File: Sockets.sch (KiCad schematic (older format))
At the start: 1 part

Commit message: Added Input Limit Switch
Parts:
- added C? (x4): C, symbol Device:C
- added D? (x2): SK35SMA, Diode_SMD:D_SMA, symbol Device:D_ALT
- added J?: LIMIT Y FRONT, Connector_JST:JST_PH_B2B-PH-K_1x02_P2.00mm_Vertical, symbol Connector:Conn_01x02_Male
- added J?: LIMIT Z UP, Connector_JST:JST_PH_B2B-PH-K_1x02_P2.00mm_Vertical, symbol Connector:Conn_01x02_Male
- added J?: LIMIT Z DOWN, Connector_JST:JST_PH_B2B-PH-K_1x02_P2.00mm_Vertical, symbol Connector:Conn_01x02_Male
- added J?: WASTE INK, Connector_JST:JST_PH_B2B-PH-K_1x02_P2.00mm_Vertical, symbol Connector:Conn_01x02_Male
- added J?: PRINTER POWER, Connector_JST:JST_PH_B2B-PH-K_1x02_P2.00mm_Vertical, symbol Connector:Conn_01x02_Male
- added J?: PE SENSOR, Connector_JST:JST_PH_B2B-PH-K_1x02_P2.00mm_Vertical, symbol Connector:Conn_01x02_Male
- added J?: LED 1, Connector_JST:JST_PH_B2B-PH-K_1x03_P2.00mm_Vertical, symbol Connector:Conn_01x03_Male
- added J?: LED 2, Connector_JST:JST_PH_B2B-PH-K_1x03_P2.00mm_Vertical, symbol Connector:Conn_01x03_Male
- added R? (x4): 1kΩ, Resistor_SMD:R_0603_1608Metric, symbol Device:R
- added R? (x4): 100kΩ, Resistor_SMD:R_0603_1608Metric, symbol Device:R
- added R? (x2): 330Ω, symbol Device:R
- added U?: 74HC245, symbol 74xx:74HC245
- J?: value Conn_01x03_Male -> LIMIT Y BACK; footprint (none) -> Connector_JST:JST_PH_B2B-PH-K_1x02_P2.00mm_Vertical; symbol Connector:Conn_01x03_Male -> Connector:Conn_01x02_Male
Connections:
- net at J?.1 (Pin_1): now also R?.1
- net GND: now reaches J?.2 (Pin_2)
- net GND: now also C?.2, C?.2, C?.2, C?.2, J?.2 (Pin_2), J?.2 (Pin_2), J?.2 (Pin_2), J?.3 (Pin_3), J?.3 (Pin_3)
- new net: J?.1 (Pin_1), R?.1 (x3)
- new net: D?.1 (K), J?.1 (Pin_1) (x2)
- new net: J?.2 (Pin_2), R?.2 (x2)
- new net +3V3: R?.2, R?.2, R?.2, R?.2
- new net +5V: D?.2 (A), D?.2 (A)
- new net LED1_CONTROL: R?.1
- new net LED2_CONTROL: R?.1
- new net LIMIT_Y_BACK: C?.1, R?.1, R?.2
- new net LIMIT_Y_FRONT: C?.1, R?.1, R?.2
- new net LIMIT_Z_DOWN: C?.1, R?.1, R?.2
- new net LIMIT_Z_UP: C?.1, R?.1, R?.2
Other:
- note added: "Złącza JST PH"
- note added: "pomyśleć nad buffoerm 74HC245 albo wersja LVC zależy od napięć"
- note added: "sprawdzić jak to podłączyć, jakie napięcia"
- note added: "wykrycie czy drukarka włączaona"
- note removed: "Złącza JST KR"

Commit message: Finished Emergency Circuit
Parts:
- removed C? (x4): C, symbol Device:C
- removed D? (x2): SK35SMA, Diode_SMD:D_SMA, symbol Device:D_ALT
- removed J?: PE SENSOR, Connector_JST:JST_PH_B2B-PH-K_1x02_P2.00mm_Vertical, symbol Connector:Conn_01x02_Male
- removed R? (x4): 1kΩ, Resistor_SMD:R_0603_1608Metric, symbol Device:R
- removed R? (x4): 100kΩ, Resistor_SMD:R_0603_1608Metric, symbol Device:R
- removed R? (x2): 330Ω, symbol Device:R
- added C? (x5): 1nF, Capacitor_SMD:C_0603_1608Metric, symbol Device:C
- added D?: 1N4448WS-7-F, symbol Device:D_ALT
- added D?: BZT52C3V3-7-F, Diode_SMD:D_SOD-123, symbol Device:D_Zener_ALT
- added D? (x2): B140-13-F, symbol Device:D_ALT
- added J?: CA58SUB-B, footprints:THT_FPC_r1.0mm_11pin_vertical, symbol Connector_Generic:Conn_01x11
- added J?: PC6 EPSON MAINBOARD, footprints:THT_FPC_r1.0mm_11pin_vertical, symbol Connector_Generic:Conn_01x11
- added J?: Y AXIS, Connector_JST:JST_PH_B2B-PH-K_1x03_P2.00mm_Vertical, symbol Connector:Conn_01x03_Male
- added J?: Z AXIS, Connector_JST:JST_PH_B2B-PH-K_1x03_P2.00mm_Vertical, symbol Connector:Conn_01x03_Male
- added J?: PHOTO SENSOR EMITER, Connector_JST:JST_PH_B2B-PH-K_1x02_P2.00mm_Vertical, symbol Connector:Conn_01x02_Male
- added J?: PHOTO SENSOR RECEIVER, Connector_JST:JST_PH_B2B-PH-K_1x03_P2.00mm_Vertical, symbol Connector:Conn_01x03_Male
- added Q? (x3): BC817, Package_TO_SOT_SMD:SOT-23, symbol Transistor_BJT:BC817
- added R?: NI, symbol Device:R
- added R? (x2): 0Ω, symbol Device:R
- added R? (x2): 10kΩ, symbol Device:R
- added R? (x3): 4.7kΩ, symbol Device:R
- added R? (x7): 1kΩ, Resistor_SMD:R_0603_1608Metric, symbol Device:R
- added R? (x5): 4.7kΩ, Resistor_SMD:R_0603_1608Metric, symbol Device:R
- added R?: 1kΩ, symbol Device:R
- added R?: NI, Resistor_SMD:R_0603_1608Metric, symbol Device:R
- added R? (x2): 10kΩ, Resistor_SMD:R_0603_1608Metric, symbol Device:R
- added RN? (x2): 330Ω, symbol Device:R_Pack04
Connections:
- net +3V3: now also R?.2, R?.2, R?.2, R?.2, R?.2, R?.2, R?.2
- net +5V: now also U?.1 (A->B), U?.20 (VCC), D?.2 (A), D?.2 (A)
- net GND: now also J?.2 (Pin_2), J?.2 (Pin_2), U?.10 (GND), U?.19 (CE), C?.2, C?.2, C?.2, C?.2, C?.2, D?.2 (A), J?.2 (Pin_2), J?.2 (Pin_2), J?.2 (Pin_2), J?.2 (Pin_2), J?.4 (Pin_4), J?.4 (Pin_4), J?.6 (Pin_6), J?.6 (Pin_6), J?.8 (Pin_8), J?.8 (Pin_8), Q?.2 (E), Q?.2 (E), Q?.2 (E), R?.1
- net LED1_CONTROL: now also U?.6 (A4)
- net LED2_CONTROL: now also U?.7 (A5)
- net LIMIT_Y_BACK: now also C?.1, R?.1
- net LIMIT_Y_FRONT: now also C?.1, R?.1
- net LIMIT_Z_DOWN: now also C?.1, R?.1
- net LIMIT_Z_UP: now also C?.1, R?.1
- net at J?.1 (Pin_1): now also R?.1, R?.2 (x5)
- net at J?.1 (Pin_1): now also R?.2
- net at J?.1 (Pin_1): now also D?.1 (K) (x2)
- net LED1_CNT: now reaches J?.2 (Pin_2)
- net LED1_CNT: now also RN?.4 (R4.1)
- net LED2_CNT: now reaches J?.2 (Pin_2)
- net LED2_CNT: now also RN?.3 (R3.1)
- net at U?.11 (B7): now also RN?.8 (R1.2)
- net at U?.12 (B6): now also RN?.7 (R2.2)
- net at U?.13 (B5): now also RN?.6 (R3.2)
- net at U?.14 (B4): now also RN?.5 (R4.2)
- net at U?.15 (B3): now also RN?.8 (R1.2)
- net at U?.16 (B2): now also RN?.7 (R2.2)
- net at U?.17 (B1): now also RN?.6 (R3.2)
- net at U?.18 (B0): now also RN?.5 (R4.2)
- net Y_STEP: now reaches U?.2 (A0)
- net Y_DIR: now reaches U?.3 (A1)
- net Z_STEP: now reaches U?.4 (A2)
- net Z_DIR: now reaches U?.5 (A3)
- new net: Q?.1 (B), R?.1 (x3)
- new net: D?.1 (K), J?.1 (Pin_1), J?.1 (Pin_1), R?.1
- new net: J?.3 (Pin_3), R?.2, R?.2, R?.2
- new net 3.3V: J?.1 (Pin_1), J?.11 (Pin_11), R?.2
- new net APG: J?.10 (Pin_10), J?.2 (Pin_2)
- new net APGHP: J?.1 (Pin_1), J?.11 (Pin_11)
- new net ENC1_A: R?.1
- new net ENC1_B: R?.1
- new net OPE: J?.3 (Pin_3), Q?.3 (C), R?.1, R?.2
- new net OPF_A: J?.5 (Pin_5), R?.2
- new net OPF_B: J?.7 (Pin_7), R?.2
- new net PC1: J?.3 (Pin_3), J?.9 (Pin_9)
- new net PE: J?.9 (Pin_9), R?.1
- new net PE_S: J?.10 (Pin_10), J?.2 (Pin_2), R?.2
- new net PE_SIGNAL: R?.2
- new net PF_A: J?.7 (Pin_7), R?.1, R?.2
- new net PF_B: J?.5 (Pin_5), R?.1, R?.2
- new net PHOTO_SENSOR: D?.1 (K), R?.1
- new net PRINTER_POWER_DETECT: Q?.3 (C), R?.1
- new net PRINTER_POWER_DETECT2: Q?.3 (C), R?.1
- new net VS: D?.2 (A)
- new net WASTE_INK: C?.1, R?.1
- new net YDIR: J?.3 (Pin_3), RN?.3 (R3.1)
- new net YSTEP: J?.1 (Pin_1), RN?.4 (R4.1)
- new net ZDIR: J?.3 (Pin_3), RN?.1 (R1.1)
- new net ZSTEP: J?.1 (Pin_1), RN?.2 (R2.1)
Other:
- note added: "Buffered outputs signals"
- note added: "Check if switching is fast enought"
- note added: "EPOSON FPC Input and Output"
- note added: "EPSON POWER DETECTION TWO WAY"
- note added: "Limit out. voltage to 3.3V"
- note added: "Limit switches input"
- note added: "Mount just one 10k resistor for corect sensor type"
- note added: "NPN Type"
- note added: "Optional Step/DIR Outputs"
- note added: "Ovecurrent protection for LED and Sensors?"
- note added: "PE Signal Output to Emulate PE Sensor"
- note added: "PNP Type"
- note added: "Photobarier sensor Input"
- note added: "RC Debounce"
- note added: "Simple ESD protection, current limit for uC interial diodes"
- note added: "Two Digital LED control signal output"
- note added: "Waste Ink Input"
- note removed: "pomyśleć nad buffoerm 74HC245 albo wersja LVC zależy od napięć"
- note removed: "sprawdzić jak to podłączyć, jakie napięcia"
- note removed: "wykrycie czy drukarka włączaona"
- moved on the sheet: J?, U?

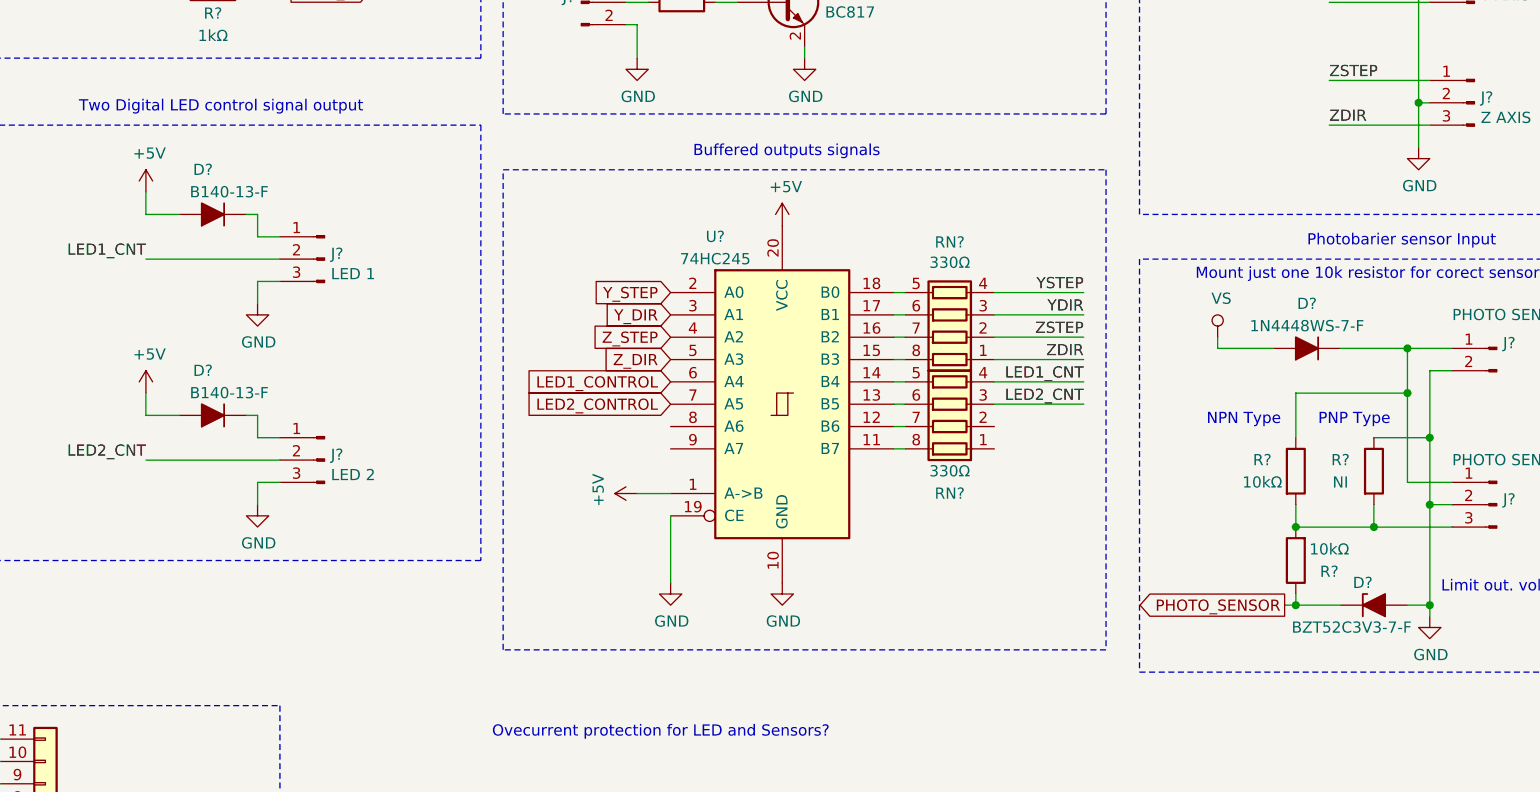
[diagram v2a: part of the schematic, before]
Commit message: Added Polyfuses and replace diodes
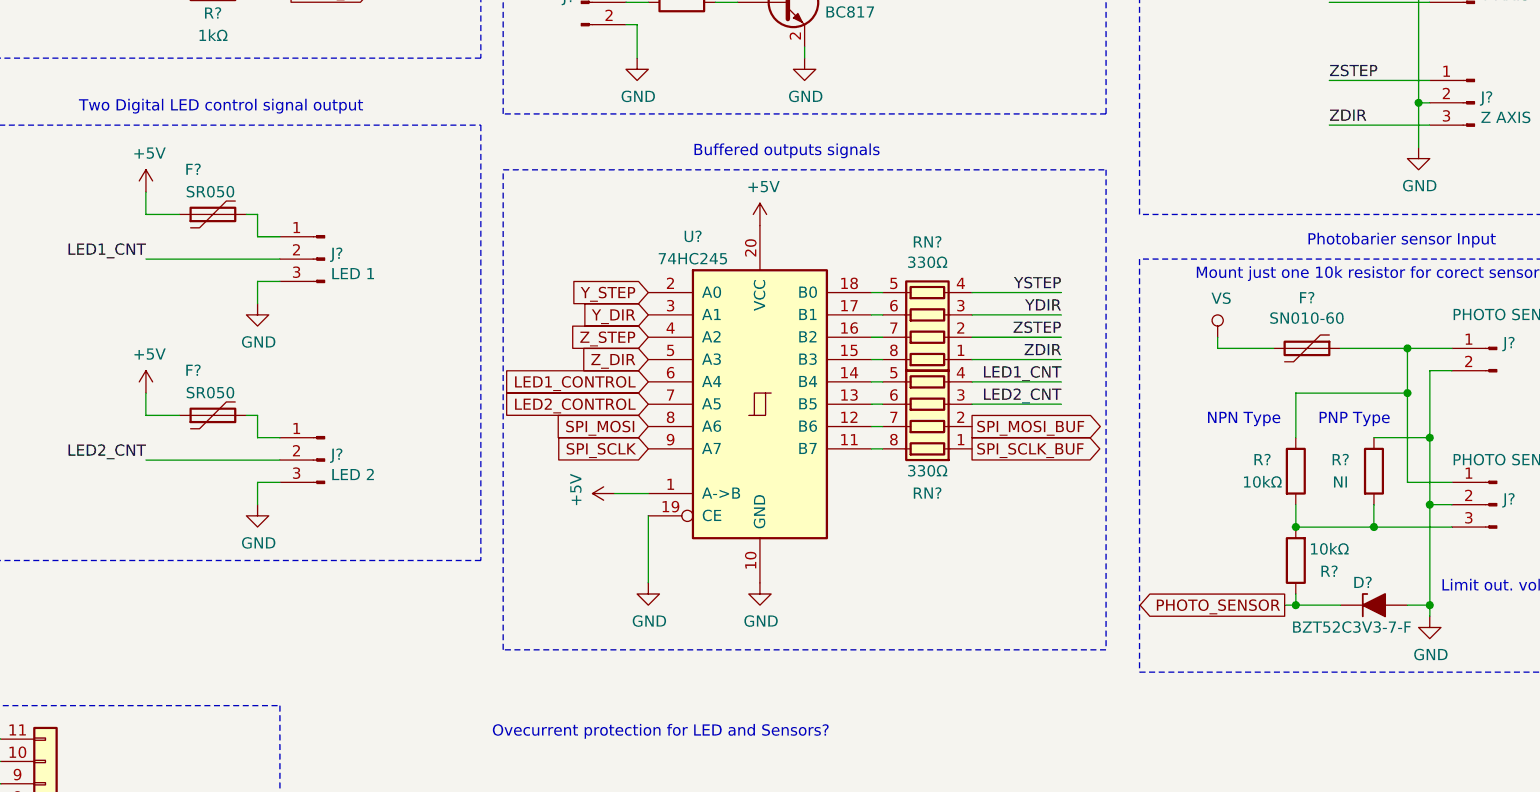
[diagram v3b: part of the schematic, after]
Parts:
- removed D?: 1N4448WS-7-F, symbol Device:D_ALT
- removed D? (x2): B140-13-F, symbol Device:D_ALT
- added F?: SN010-60, Fuse:Fuse_1206_3216Metric, symbol Device:Polyfuse
- added F? (x2): SR050, Fuse:Fuse_0805_2012Metric, symbol Device:Polyfuse
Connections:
- net +5V: now also F?.1, F?.1
- net VS: now also F?.2
- net at J?.1 (Pin_1): now also F?.2 (x2)
- net SPI_MOSI: now reaches U?.8 (A6)
- net SPI_SCLK: now reaches U?.9 (A7)
- net SPI_SCLK_BUF: now reaches RN?.1 (R1.1)
- net SPI_MOSI_BUF: now reaches RN?.2 (R2.1)
- net at J?.1 (Pin_1), J?.1 (Pin_1), R?.1: now also F?.1
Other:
- moved on the sheet: RN?, U?
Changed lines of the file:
@@
 $Descr A4 11693 8268
 encoding utf-8
-Sheet 5 9
+Sheet 5 10
 Title ""
 Date ""
@@
 L 74xx:74HC245 U?
 U 1 1 5E1776F2
-P 6900 4700
+P 6800 4700
 AR Path="/5E07245F/5E1776F2" Ref="U?"  Part="1"
 AR Path="/5E858220/5E1776F2" Ref="U?"  Part="1"
-F 0 "U?" H 6600 5450 50  0000 C CNN
-F 1 "74HC245" H 6600 5350 50  0000 C CNN
-F 2 "" H 6900 4700 50  0001 C CNN
-F 3 "http://www.ti.com/lit/gpn/sn74HC245" H 6900 4700 50  0001 C CNN
-	1    6900 4700
+F 0 "U?" H 6500 5450 50  0000 C CNN
+F 1 "74HC245" H 6500 5350 50  0000 C CNN
+F 2 "" H 6800 4700 50  0001 C CNN
+F 3 "http://www.ti.com/lit/gpn/sn74HC245" H 6800 4700 50  0001 C CNN
+	1    6800 4700
 	1    0    0    -1
 $EndComp
@@
 	-1   0    0    -1
 $EndComp
-Text GLabel 6400 4200 0    50   Input ~ 0
+Text GLabel 6300 4200 0    50   Input ~ 0
 Y_STEP
-Text GLabel 6400 4300 0    50   Input ~ 0
+Text GLabel 6300 4300 0    50   Input ~ 0
 Y_DIR
-Text GLabel 6400 4400 0    50   Input ~ 0
+Text GLabel 6300 4400 0    50   Input ~ 0
 Z_STEP
-Text GLabel 6400 4500 0    50   Input ~ 0
+Text GLabel 6300 4500 0    50   Input ~ 0
 Z_DIR
-Text GLabel 6400 4600 0    50   Input ~ 0
+Text GLabel 6300 4600 0    50   Input ~ 0
 LED1_CONTROL
-Text GLabel 6400 4700 0    50   Input ~ 0
+Text GLabel 6300 4700 0    50   Input ~ 0
 LED2_CONTROL
 $Comp
 L power:+5V #PWR?
 U 1 1 5E6328B5
-P 6900 3900
+P 6800 3900
 AR Path="/5E07245F/5E6328B5" Ref="#PWR?"  Part="1"
 AR Path="/5E858220/5E6328B5" Ref="#PWR?"  Part="1"
-F 0 "#PWR?" H 6900 3750 50  0001 C CNN
-F 1 "+5V" H 6915 4073 50  0000 C CNN
-F 2 "" H 6900 3900 50  0001 C CNN
-F 3 "" H 6900 3900 50  0001 C CNN
-	1    6900 3900
+F 0 "#PWR?" H 6800 3750 50  0001 C CNN
+F 1 "+5V" H 6815 4073 50  0000 C CNN
+F 2 "" H 6800 3900 50  0001 C CNN
+F 3 "" H 6800 3900 50  0001 C CNN
+	1    6800 3900
 	1    0    0    -1
 $EndComp
@@
 L power:GND #PWR?
 U 1 1 5E632F5F
-P 6900 5500
+P 6800 5500
 AR Path="/5E07245F/5E632F5F" Ref="#PWR?"  Part="1"
 AR Path="/5E858220/5E632F5F" Ref="#PWR?"  Part="1"
-F 0 "#PWR?" H 6900 5250 50  0001 C CNN
-F 1 "GND" H 6905 5327 50  0000 C CNN
-F 2 "" H 6900 5500 50  0001 C CNN
-F 3 "" H 6900 5500 50  0001 C CNN
-	1    6900 5500
+F 0 "#PWR?" H 6800 5250 50  0001 C CNN
+F 1 "GND" H 6805 5327 50  0000 C CNN
+F 2 "" H 6800 5500 50  0001 C CNN
+F 3 "" H 6800 5500 50  0001 C CNN
+	1    6800 5500
 	1    0    0    -1
 $EndComp
@@
 L power:GND #PWR?
 U 1 1 5E633872
-P 6400 5500
+P 6300 5500
 AR Path="/5E07245F/5E633872" Ref="#PWR?"  Part="1"
 AR Path="/5E858220/5E633872" Ref="#PWR?"  Part="1"
-F 0 "#PWR?" H 6400 5250 50  0001 C CNN
-F 1 "GND" H 6405 5327 50  0000 C CNN
-F 2 "" H 6400 5500 50  0001 C CNN
-F 3 "" H 6400 5500 50  0001 C CNN
-	1    6400 5500
-	1    0    0    -1
-$EndComp
-Wire Wire Line
-	6400 5200 6400 5500
+F 0 "#PWR?" H 6300 5250 50  0001 C CNN
+F 1 "GND" H 6305 5327 50  0000 C CNN
+F 2 "" H 6300 5500 50  0001 C CNN
+F 3 "" H 6300 5500 50  0001 C CNN
+	1    6300 5500
+	1    0    0    -1
+$EndComp
+Wire Wire Line
+	6300 5200 6300 5500
 $Comp
 L power:+5V #PWR?
 U 1 1 5E638CA6
-P 6250 5100
+P 6150 5100
 AR Path="/5E07245F/5E638CA6" Ref="#PWR?"  Part="1"
 AR Path="/5E858220/5E638CA6" Ref="#PWR?"  Part="1"
-F 0 "#PWR?" H 6250 4950 50  0001 C CNN
-F 1 "+5V" H 6265 5273 50  0000 C CNN
-F 2 "" H 6250 5100 50  0001 C CNN
-F 3 "" H 6250 5100 50  0001 C CNN
-	1    6250 5100
+F 0 "#PWR?" H 6150 4950 50  0001 C CNN
+F 1 "+5V" H 6165 5273 50  0000 C CNN
+F 2 "" H 6150 5100 50  0001 C CNN
+F 3 "" H 6150 5100 50  0001 C CNN
+	1    6150 5100
 	0    -1   -1   0
 $EndComp
 Wire Wire Line
-	6250 5100 6400 5100
-Text Label 8250 4200 2    50   ~ 0
+	6150 5100 6300 5100
+Text Label 8150 4200 2    50   ~ 0
 YSTEP
-Text Label 8250 4300 2    50   ~ 0
+Text Label 8150 4300 2    50   ~ 0
 YDIR
-Text Label 8250 4400 2    50   ~ 0
+Text Label 8150 4400 2    50   ~ 0
 ZSTEP
-Text Label 8250 4500 2    50   ~ 0
+Text Label 8150 4500 2    50   ~ 0
 ZDIR
-Text Label 8250 4600 2    50   ~ 0
+Text Label 8150 4600 2    50   ~ 0
 LED1_CNT
-Text Label 8250 4700 2    50   ~ 0
+Text Label 8150 4700 2    50   ~ 0
 LED2_CNT
 Text Label 4050 4050 2    50   ~ 0
@@
 L Device:R_Pack04 RN?
 U 1 1 5E67B210
-P 7650 4300
+P 7550 4300
 AR Path="/5E07245F/5E67B210" Ref="RN?"  Part="1"
 AR Path="/5E858220/5E67B210" Ref="RN?"  Part="1"
-F 0 "RN?" V 7975 4300 50  0000 C CNN
-F 1 "330Ω" V 7884 4300 50  0000 C CNN
-F 2 "" V 7925 4300 50  0001 C CNN
-F 3 "~" H 7650 4300 50  0001 C CNN
-	1    7650 4300
+F 0 "RN?" V 7875 4300 50  0000 C CNN
+F 1 "330Ω" V 7784 4300 50  0000 C CNN
+F 2 "" V 7825 4300 50  0001 C CNN
+F 3 "~" H 7550 4300 50  0001 C CNN
+	1    7550 4300
 	0    -1   -1   0
 $EndComp
@@
 L Device:R_Pack04 RN?
 U 1 1 5E67C616
-P 7650 4700
+P 7550 4700
 AR Path="/5E07245F/5E67C616" Ref="RN?"  Part="1"
 AR Path="/5E858220/5E67C616" Ref="RN?"  Part="1"
-F 0 "RN?" V 7250 4700 50  0000 C CNN
-F 1 "330Ω" V 7350 4700 50  0000 C CNN
-F 2 "" V 7925 4700 50  0001 C CNN
-F 3 "~" H 7650 4700 50  0001 C CNN
-	1    7650 4700
+F 0 "RN?" V 7150 4700 50  0000 C CNN
+F 1 "330Ω" V 7250 4700 50  0000 C CNN
+F 2 "" V 7825 4700 50  0001 C CNN
+F 3 "~" H 7550 4700 50  0001 C CNN
+	1    7550 4700
 	0    -1   -1   0
 $EndComp
@@
 	4050 4950 4650 4950
 Wire Wire Line
-	7400 4200 7450 4200
-Wire Wire Line
-	7450 4300 7400 4300
-Wire Wire Line
-	7400 4400 7450 4400
-Wire Wire Line
-	7400 4500 7450 4500
-Wire Wire Line
-	7400 4600 7450 4600
-Wire Wire Line
-	7400 4700 7450 4700
-Wire Wire Line
-	7400 4800 7450 4800
-Wire Wire Line
-	7400 4900 7450 4900
-Wire Wire Line
-	7850 4200 8250 4200
-Wire Wire Line
-	7850 4300 8250 4300
-Wire Wire Line
-	7850 4400 8250 4400
-Wire Wire Line
-	7850 4500 8250 4500
-Wire Wire Line
-	7850 4600 8250 4600
-Wire Wire Line
-	7850 4700 8250 4700
+	7300 4200 7350 4200
+Wire Wire Line
+	7350 4300 7300 4300
+Wire Wire Line
+	7300 4400 7350 4400
+Wire Wire Line
+	7300 4500 7350 4500
+Wire Wire Line
+	7300 4600 7350 4600
+Wire Wire Line
+	7300 4700 7350 4700
+Wire Wire Line
+	7300 4800 7350 4800
+Wire Wire Line
+	7300 4900 7350 4900
+Wire Wire Line
+	7750 4200 8150 4200
+Wire Wire Line
+	7750 4300 8150 4300
+Wire Wire Line
+	7750 4400 8150 4400
+Wire Wire Line
+	7750 4500 8150 4500
+Wire Wire Line
+	7750 4600 8150 4600
+Wire Wire Line
+	7750 4700 8150 4700
 Wire Notes Line
 	5650 3650 8350 3650
@@
 Wire Wire Line
 	9100 4450 8850 4450
-$Comp
-L Device:D_ALT D?
-U 1 1 5E7BD4E4
-P 9250 4450
-AR Path="/5E1018C2/5E7BD4E4" Ref="D?"  Part="1"
-AR Path="/5E07245F/5E7BD4E4" Ref="D?"  Part="1"
-AR Path="/5E858220/5E7BD4E4" Ref="D?"  Part="1"
-F 0 "D?" H 9250 4250 50  0000 C CNN
-F 1 "1N4448WS-7-F" H 9250 4350 50  0000 C CNN
-F 2 "" H 9250 4450 50  0001 C CNN
-F 3 "~" H 9250 4450 50  0001 C CNN
-	1    9250 4450
-	-1   0    0    1
-$EndComp
 Wire Wire Line
 	9400 4450 9700 4450
@@
 Text Notes 9250 4000 0    50   ~ 0
 Photobarier sensor Input
-$Comp
-L Device:D_ALT D?
-U 1 1 5E90B268
+Text Notes 5600 6200 0    50   ~ 0
+Ovecurrent protection for LED and Sensors?
+Text GLabel 6300 4900 0    50   Input ~ 0
+SPI_SCLK
+Text GLabel 6300 4800 0    50   Input ~ 0
+SPI_MOSI
+Text GLabel 7750 4800 2    50   Output ~ 0
+SPI_MOSI_BUF
+Text GLabel 7750 4900 2    50   Output ~ 0
+SPI_SCLK_BUF
+$Comp
+L Device:Polyfuse F?
+U 1 1 5E15436A
+P 9250 4450
+F 0 "F?" V 9025 4450 50  0000 C CNN
+F 1 "SN010-60 " V 9116 4450 50  0000 C CNN
+F 2 "Fuse:Fuse_1206_3216Metric" H 9300 4250 50  0001 L CNN
+F 3 "~" H 9250 4450 50  0001 C CNN
+	1    9250 4450
+	0    1    1    0
+$EndComp
+$Comp
+L Device:Polyfuse F?
+U 1 1 5E1588DB
+P 4350 4750
+AR Path="/5E91D96F/5E1588DB" Ref="F?"  Part="1"
+AR Path="/5E07245F/5E1588DB" Ref="F?"  Part="1"
+F 0 "F?" V 4550 4800 50  0000 L CNN
+F 1 "SR050" V 4450 4650 50  0000 L CNN
+F 2 "Fuse:Fuse_0805_2012Metric" H 4400 4550 50  0001 L CNN
+F 3 "~" H 4350 4750 50  0001 C CNN
+	1    4350 4750
+	0    -1   -1   0
+$EndComp
+$Comp
+L Device:Polyfuse F?
+U 1 1 5E1601CB
 P 4350 3850
-AR Path="/5E1018C2/5E90B268" Ref="D?"  Part="1"
-AR Path="/5E07245F/5E90B268" Ref="D?"  Part="1"
-F 0 "D?" H 4350 3650 50  0000 L CNN
-F 1 "B140-13-F" H 4100 3750 50  0000 L CNN
-F 2 "" H 4350 3850 50  0001 C CNN
+AR Path="/5E91D96F/5E1601CB" Ref="F?"  Part="1"
+AR Path="/5E07245F/5E1601CB" Ref="F?"  Part="1"
+F 0 "F?" V 4550 3900 50  0000 L CNN
+F 1 "SR050" V 4450 3750 50  0000 L CNN
+F 2 "Fuse:Fuse_0805_2012Metric" H 4400 3650 50  0001 L CNN
 F 3 "~" H 4350 3850 50  0001 C CNN
 	1    4350 3850
-	-1   0    0    1
-$EndComp
-$Comp
-L Device:D_ALT D?
-U 1 1 5E91272E
-P 4350 4750
-AR Path="/5E1018C2/5E91272E" Ref="D?"  Part="1"
-AR Path="/5E07245F/5E91272E" Ref="D?"  Part="1"
-F 0 "D?" H 4350 4550 50  0000 L CNN
-F 1 "B140-13-F" H 4100 4650 50  0000 L CNN
-F 2 "" H 4350 4750 50  0001 C CNN
-F 3 "~" H 4350 4750 50  0001 C CNN
-	1    4350 4750
-	-1   0    0    1
-$EndComp
-Text Notes 5600 6200 0    50   ~ 0
-Ovecurrent protection for LED and Sensors?
+	0    -1   -1   0
+$EndComp
 $EndSCHEMATC
